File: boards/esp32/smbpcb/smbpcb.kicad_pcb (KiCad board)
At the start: 2 copper layers, 72.1 x 53.3 mm, 54 parts, among them IC1 MiCS-6814, J1 USB_B_Micro, Q1 SUD08P06-155L, Q2 SS8050_NPN, Q3 SS8050_NPN, U1 MCP73831-2-OT, U2 TPS61200DRC, U3 ESP32-WROOM-32, U4 SSD1306, U5 BME680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

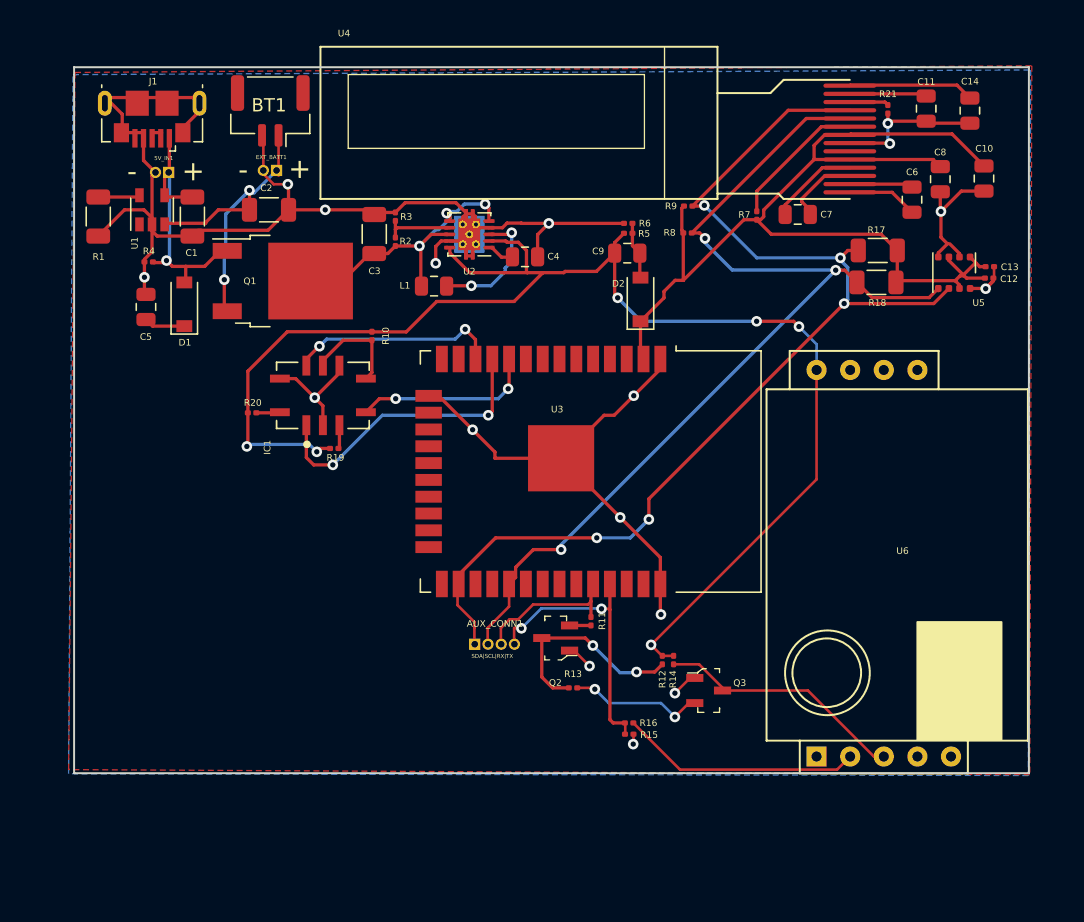
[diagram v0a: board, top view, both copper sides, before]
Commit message: pms7003 time
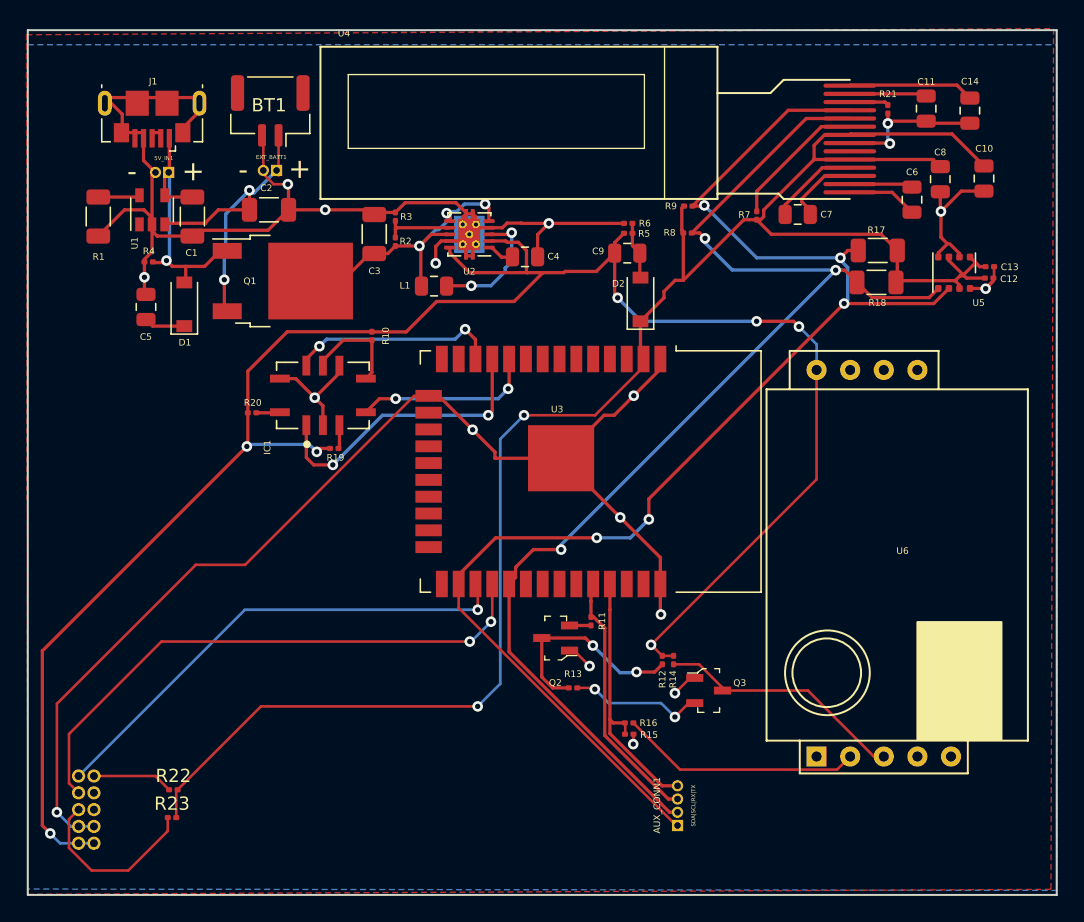
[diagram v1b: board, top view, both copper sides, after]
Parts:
- added J2: PMS7003, mics:PMS7003, F.Cu at (96.3, 63.3)
- added R22: 10k, Capacitor_SMD:C_0201_0603Metric, F.Cu at (85.2, 72.3)
- added R23: 10k, Capacitor_SMD:C_0201_0603Metric, F.Cu at (85.1, 74.4)
- moved AUX_CONN1 20.6 mm to (123.3, 75.0), turned to 180 degrees
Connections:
- net ESP_RX renamed ESP_RX0
- net ESP_TX renamed ESP_TX0
- U3 pad 27: unconnected-(U3-Pad27) -> ESP_TX1
- U3 pad 28: unconnected-(U3-Pad28) -> ESP_RX1
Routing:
- net +3V3: track 78.5 -> 140.5 mm, vias 0 -> 2
- net GND: track 160.2 -> 209.3 mm, vias 17 -> 18
- net ESP_RX1: track 0.00 -> 43.0 mm, vias 0 -> 2
- net +5V: track 108.2 -> 147.8 mm, vias 6 -> 7
- net ESP_TX1: track 0.00 -> 37.4 mm, vias 0 -> 1
- net SDA: track 86.1 -> 106.1 mm
- net SCL: track 77.7 -> 95.4 mm
- net Net-(J2-Pad5): track 0.00 -> 13.6 mm
- net ESP_RX0: track 11.2 -> 19.3 mm
- net Net-(J2-Pad10): track 0.00 -> 6.11 mm
- net ESP_TX0: track 21.5 -> 20.2 mm, vias 2 -> 0
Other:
- board size 72.1 x 53.3 mm -> 77.7 x 65.3 mm

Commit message: more work'
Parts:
- added ?: , , F.Cu at (74.1, 78.1)
- added AUX_CONN2: Conn_01x04_Female, Connector_PinHeader_1.00mm:PinHeader_1x04_P1.00mm_Vertical, F.Cu at (127.0, 75.0)
- added AUX_CONN3: Conn_01x04_Female, Connector_PinHeader_1.00mm:PinHeader_1x04_P1.00mm_Vertical, F.Cu at (130.6, 75.0)
- added AUX_CONN4: Conn_01x04_Female, Connector_PinHeader_1.00mm:PinHeader_1x04_P1.00mm_Vertical, F.Cu at (133.9, 75.0)
- added C15: 1nF, Capacitor_SMD:C_0201_0603Metric, F.Cu at (101.9, 52.9)
- added C16: 1nF, Capacitor_SMD:C_0201_0603Metric, F.Cu at (84.5, 50.6)
- added D3: PWR_LED, LED_SMD:LED_0805_2012Metric, F.Cu at (88.2, 39.8)
- added D4: PWR_LED, LED_SMD:LED_0805_2012Metric, F.Cu at (80.2, 39.8)
- added D5: D_Schottky, Diode_SMD:D_SOD-123, F.Cu at (80.2, 23.9)
- added R24: 470, Capacitor_SMD:C_0201_0603Metric, F.Cu at (101.8, 55.4)
- added R25: 2k, Capacitor_SMD:C_0201_0603Metric, F.Cu at (91.0, 39.2)
- added R26: 470, Capacitor_SMD:C_0201_0603Metric, F.Cu at (85.4, 48.5)
- added R27: 5.1k, Capacitor_SMD:C_0201_0603Metric, F.Cu at (101.8, 57.7)
- added R28: 470, Capacitor_SMD:C_0201_0603Metric, F.Cu at (83.3, 39.9)
- added REF**: MountingHole_3.2mm_M3_ISO7380_Pad, mountingholes:MountingHole_3.2mm_M3_ISO7380_Pad, F.Cu at (148.5, 16.5)
- added REF**: MountingHole_3.2mm_M3_ISO7380_Pad, mountingholes:MountingHole_3.2mm_M3_ISO7380_Pad, F.Cu at (147.7, 77.9)
- added REF**: MountingHole_3.2mm_M3_ISO7380_Pad, mountingholes:MountingHole_3.2mm_M3_ISO7380_Pad, F.Cu at (73.6, 16.6)
- added SW1: RESET, Button_Switch_SMD:SW_SPST_Omron_B3FS-101xP, F.Cu at (95.2, 54.8)
- added SW2: RESET, Button_Switch_SMD:SW_SPST_Omron_B3FS-101xP, F.Cu at (84.3, 54.9)
- BT1: footprint Connector_JST:JST_GH_SM02B-GHS-TB_1x02-1MP_P1.25mm_Horizontal -> Connector_JST:JST_EH_S2B-EH_1x02_P2.50mm_Horizontal
- R1: value 10k -> 2k
- moved J1 11.0 mm to (73.2, 25.1), turned to -90 degrees
- moved 5V_IN1 8.02 mm to (77.0, 24.2), turned to 0 degrees
- moved EXT_BATT1 4.12 mm to (91.3, 21.8), turned to 90 degrees
- moved R1 3.62 mm to (79.5, 32.6), turned to 0 degrees
- moved BT1 2.72 mm to (90.5, 19.1), turned to 0 degrees
- moved C2 0.22 mm to (92.5, 28.7)
- moved U1 0.15 mm to (83.5, 28.4)
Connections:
- AUX_CONN1 pad 3: ESP_RX0 -> ESP_TX0
- AUX_CONN1 pad 4: ESP_TX0 -> ESP_RX0
- C1 pad 1: Net-(5V_IN1-Pad1) -> Net-(C1-Pad1)
- D1 pad 2: Net-(5V_IN1-Pad1) -> Net-(C1-Pad1)
- J2 pad 7: ESP_RX1 -> ESP_RX2
- J2 pad 9: ESP_TX1 -> ESP_TX2
- Q1 pad 1: Net-(5V_IN1-Pad1) -> Net-(C1-Pad1)
- R11 pad 1: ESP_RX0 -> ESP_RX1
- R15 pad 2: ESP_TX0 -> ESP_TX1
- R16 pad 1: ESP_TX0 -> ESP_TX1
- R4 pad 1: Net-(5V_IN1-Pad1) -> Net-(C1-Pad1)
- U1 pad 1: unconnected-(U1-Pad1) -> Net-(D4-Pad1)
- U1 pad 4: Net-(5V_IN1-Pad1) -> Net-(C1-Pad1)
- U3 pad 10: NH3 -> unconnected-(U3-Pad10)
- U3 pad 11: NO2 -> unconnected-(U3-Pad11)
- U3 pad 12: CO -> unconnected-(U3-Pad12)
- U3 pad 25: unconnected-(U3-Pad25) -> IO0
- U3 pad 27: ESP_TX1 -> ESP_TX2
- U3 pad 28: ESP_RX1 -> ESP_RX2
- U3 pad 3: unconnected-(U3-Pad3) -> EN
- U3 pad 36: unconnected-(U3-Pad36) -> ESP_TX1
- U3 pad 37: unconnected-(U3-Pad37) -> ESP_RX1
- U3 pad 6: unconnected-(U3-Pad6) -> CO
- U3 pad 8: unconnected-(U3-Pad8) -> NH3
- U3 pad 9: unconnected-(U3-Pad9) -> NO2
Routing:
- net +3V3: track 140.5 -> 186.7 mm, vias 2 -> 3
- net ESP_RX2: track 0.00 -> 43.0 mm, vias 0 -> 2
- net EN: track 0.00 -> 38.1 mm, vias 0 -> 2
- net ESP_TX2: track 0.00 -> 37.4 mm, vias 0 -> 1
- net ESP_RX1: track 43.0 -> 5.72 mm, vias 2 -> 0
- net Net-(C1-Pad1): track 0.00 -> 29.1 mm, vias 0 -> 4
- net GND: track 209.3 -> 237.9 mm, vias 18 -> 19
- net ESP_TX1: track 37.4 -> 11.9 mm, vias 1 -> 2
- net Net-(5V_IN1-Pad1): track 20.6 -> 4.37 mm, vias 1 -> 0
- net Net-(D4-Pad1): track 0.00 -> 12.2 mm, vias 0 -> 2
- net SCL: track 95.4 -> 107.0 mm
- net SDA: track 106.1 -> 117.7 mm
- net +5V: track 147.8 -> 137.8 mm, vias 7 -> 5
- net CO: track 15.5 -> 23.1 mm
- net Net-(C16-Pad2): track 0.00 -> 7.12 mm
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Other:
- board size 77.7 x 65.3 mm -> 81.9 x 69.8 mm
- board text added: "CHG_LED"
- board text added: "IO0"
- board text added: "PWR_LED"
- board text added: "SDA|SCL|3V3|GND"
- board text added: "SDA|SCL|5V|GND"
- board text added: "SDA|SCL|TX|RX"
- board text removed: "SDA|SCL|RX|TX"

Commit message: ordering dis
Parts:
- R17, R18: footprint Capacitor_SMD:C_1206_3216Metric -> Capacitor_SMD:C_0805_2012Metric
- R22, R23, R27, R4, R7, R8, R9: footprint Capacitor_SMD:C_0201_0603Metric -> Capacitor_SMD:C_0805_2012Metric
- moved R27 1.65 mm to (101.8, 59.4)
- moved R8 0.91 mm to (123.7, 31.1)
- moved R9 0.79 mm to (123.8, 28.9)
- moved R4 0.55 mm to (83.7, 32.0)
- moved D3 0.31 mm to (88.3, 40.0)
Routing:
- net GND: track 237.9 -> 252.2 mm
- net +5V: track 137.8 -> 130.9 mm, vias 5 -> 11
- net +3V3: track 186.7 -> 188.7 mm
- net IO0: track 5.74 -> 7.03 mm
- net SCL: track 107.0 -> 105.8 mm

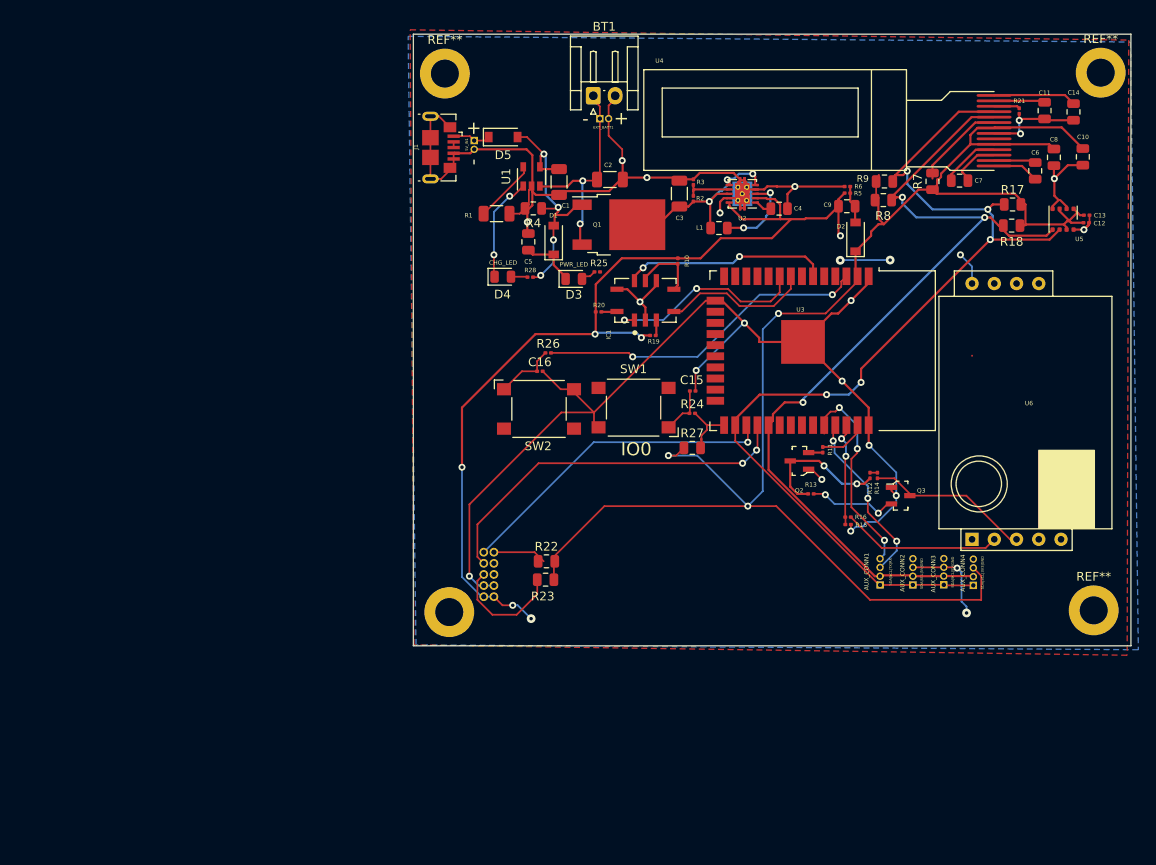
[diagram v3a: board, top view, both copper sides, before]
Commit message: added decoupling cap to 3v3 off of esp32 board
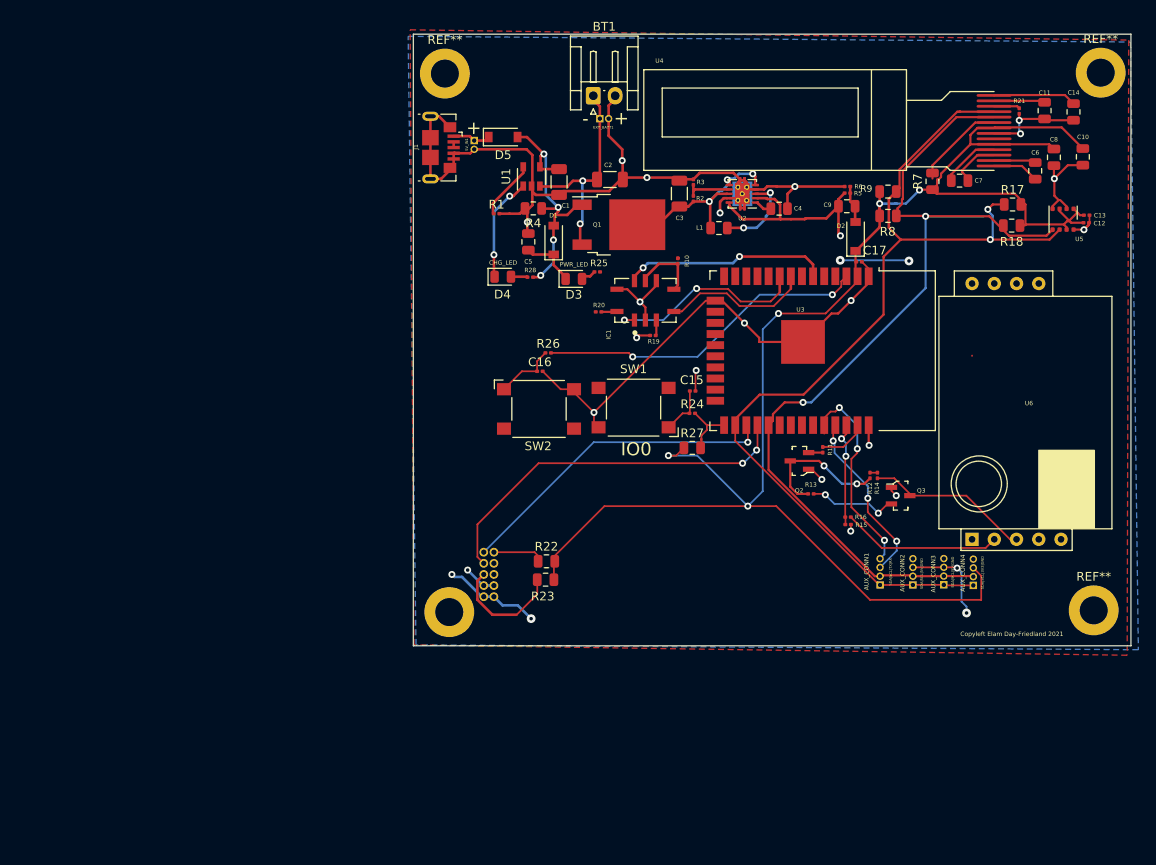
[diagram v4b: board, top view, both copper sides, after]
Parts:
- added C17: 10uF, Capacitor_SMD:C_0201_0603Metric, F.Cu at (120.9, 38.1)
- R1: footprint Capacitor_SMD:C_1206_3216Metric -> Capacitor_SMD:C_0201_0603Metric
- moved R8 1.88 mm to (124.2, 32.9)
- moved R9 1.22 mm to (124.2, 30.1)
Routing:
- net +5V: track 130.9 -> 56.4 mm, vias 11 -> 8
- net GND: track 252.2 -> 191.9 mm
- net SCL: track 105.8 -> 111.1 mm, vias 3 -> 2
- net SDA: track 117.7 -> 114.8 mm, vias 5 -> 2
- net +3V3: track 188.7 -> 187.4 mm, vias 3 -> 5
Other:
- board text added: "Copyleft Elam Day-Friedland 2021"

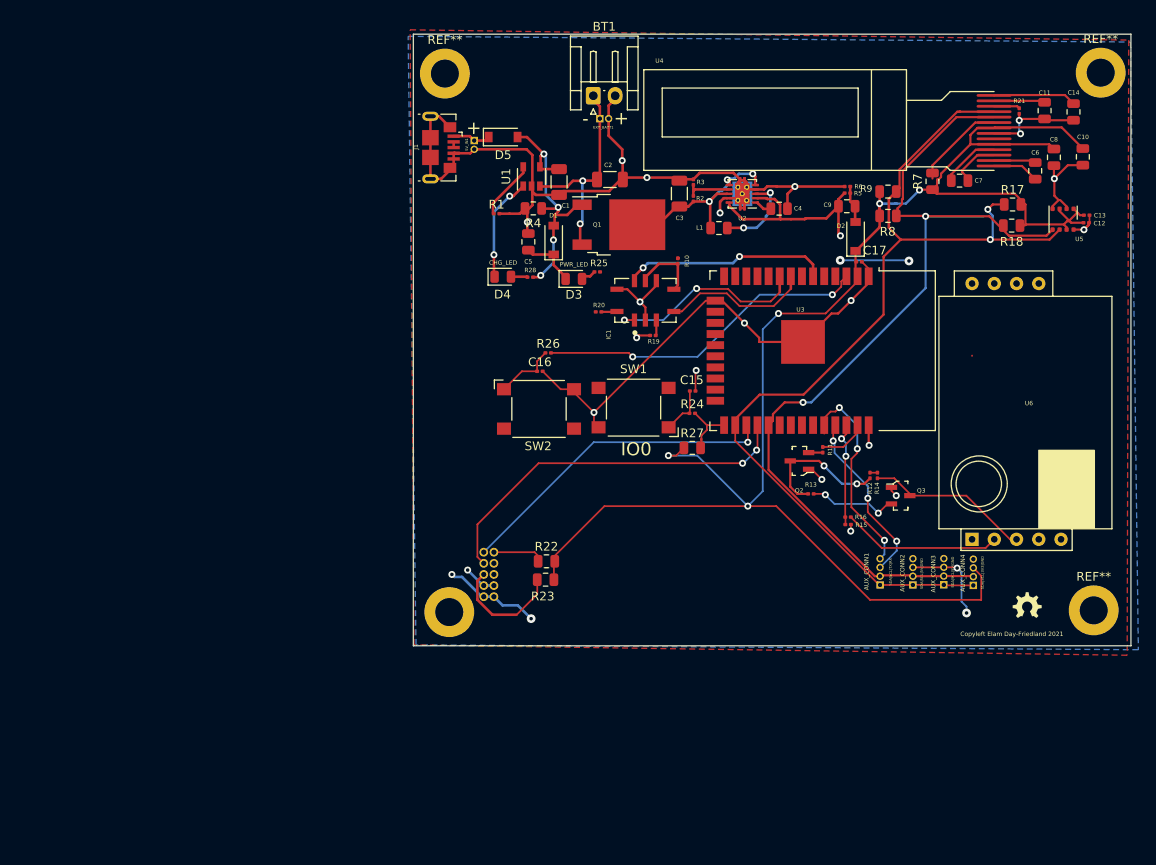
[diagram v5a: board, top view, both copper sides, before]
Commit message: made everything 0805 or bigger except that nagging BGA Linear regulator and the bme680
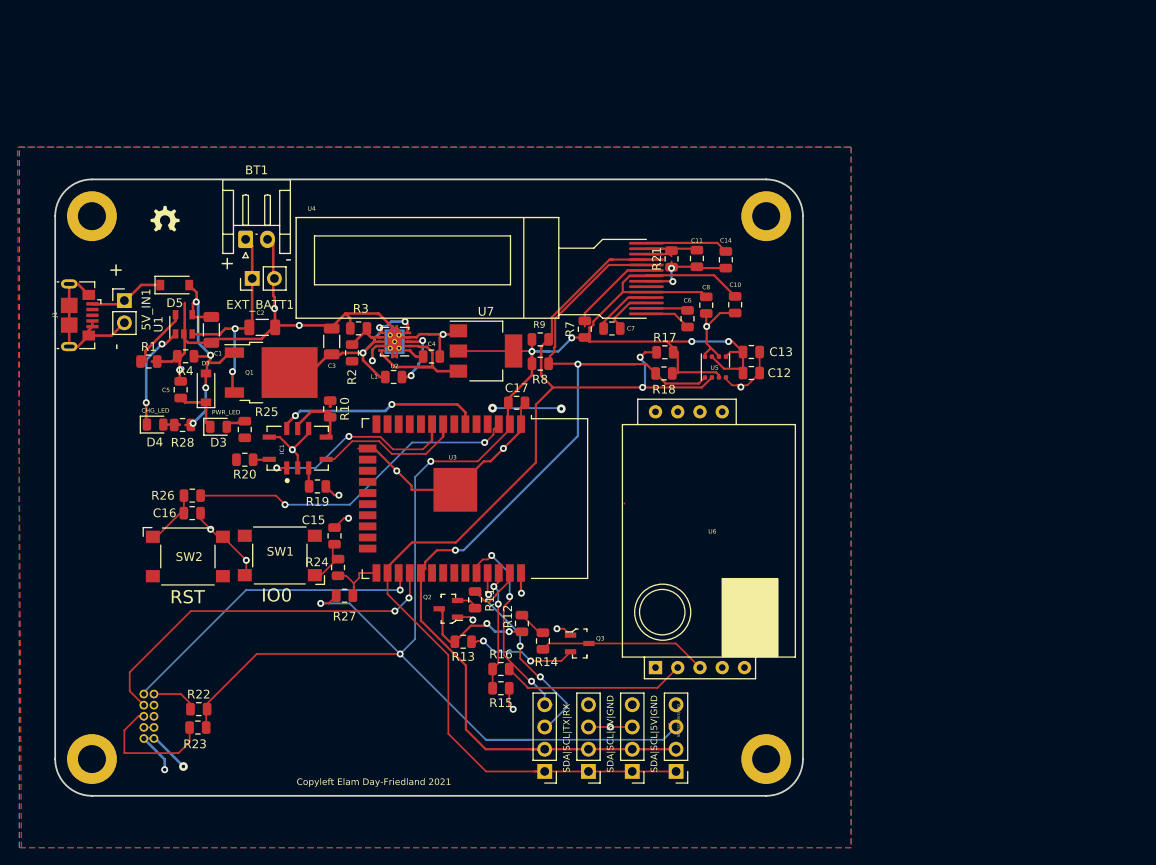
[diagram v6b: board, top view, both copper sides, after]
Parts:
- removed C9: 22pF, Capacitor_SMD:C_0805_2012Metric
- removed D2: D, Diode_SMD:D_SOD-123
- removed R5: 1k, Capacitor_SMD:C_0201_0603Metric
- removed R6: 2k, Capacitor_SMD:C_0201_0603Metric
- removed the REF** at (148.5, 16.5)
- removed the REF** at (147.7, 77.9)
- removed the REF** at (73.6, 16.6)
- added MOUNT4: MountingHole_3.2mm_M3_ISO7380_Pad, MountingHole:MountingHole_3.2mm_M3_ISO7380_Pad, F.Cu at (110.3, 94.9)
- added REF**: MountingHole_3.2mm_M3_ISO7380_Pad, MountingHole:MountingHole_3.2mm_M3_ISO7380_Pad, F.Cu at (110.3, 32.9)
- added REF**: MountingHole_3.2mm_M3_ISO7380_Pad, MountingHole:MountingHole_3.2mm_M3_ISO7380_Pad, F.Cu at (33.3, 32.9)
- added U7: AMS1117-3.3, Package_TO_SOT_SMD:SOT-223-3_TabPin2, F.Cu at (78.3, 48.3)
- 5V_IN1, EXT_BATT1: footprint Connector_PinHeader_1.00mm:PinHeader_1x02_P1.00mm_Vertical -> Connector_PinHeader_2.54mm:PinHeader_1x02_P2.54mm_Vertical
- AUX_CONN1, AUX_CONN2, AUX_CONN3, AUX_CONN4: footprint Connector_PinHeader_1.00mm:PinHeader_1x04_P1.00mm_Vertical -> Connector_PinHeader_2.54mm:PinHeader_1x04_P2.54mm_Vertical
- C12, C13: value .1uF -> 100nF; footprint Capacitor_SMD:C_0201_0603Metric -> Capacitor_SMD:C_0805_2012Metric
- C15, C16, C17, R1, R10, R11, R12, R13, R14, R15, R16, R19, R2, R20, R21, R24, R25, R26, R28, R3: footprint Capacitor_SMD:C_0201_0603Metric -> Capacitor_SMD:C_0805_2012Metric
- moved J1 45.5 mm to (31.9, 44.2)
- moved C15 44.1 mm to (61.0, 69.4), turned to -90 degrees
- moved R24 44.1 mm to (61.4, 73.0), turned to -90 degrees
- moved R25 44.1 mm to (50.8, 57.2), turned to -90 degrees
- moved D3 43.9 mm to (47.8, 56.9)
- moved 5V_IN1 43.9 mm to (37.0, 42.5)
- moved R15 43.8 mm to (80.0, 86.8)
- moved AUX_CONN1 43.8 mm to (85.0, 96.3)
- moved R26 43.8 mm to (44.8, 64.8)
- moved R20 43.8 mm to (50.8, 60.7)
- moved SW1 43.8 mm to (54.8, 71.6)
- moved EXT_BATT1 43.7 mm to (51.6, 40.0)
- moved Q2 43.5 mm to (74.0, 77.7)
- moved SW2 43.5 mm to (44.2, 71.8)
- moved R16 43.3 mm to (80.0, 84.6)
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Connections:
- ? pad 1: (no net) -> GND
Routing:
- net +3V3: track 187.4 -> 213.6 mm, vias 5 -> 7
- net GND: track 191.9 -> 171.1 mm
- net SDA: track 114.8 -> 129.1 mm
- net SCL: track 111.1 -> 124.0 mm
- net +5V: track 56.4 -> 45.0 mm, vias 8 -> 6
- net Net-(C9-Pad2): track 4.28 -> 0.00 mm
- net Net-(5V_IN1-Pad1): track 4.37 -> 8.59 mm
- net Net-(R16-Pad2): track 18.3 -> 21.2 mm
- net ESP_TX0: track 20.4 -> 23.3 mm
- net Net-(Q3-Pad2): track 10.2 -> 12.7 mm
- net Net-(L1-Pad2): track 10.1 -> 7.72 mm
- net ESP_RX1: track 5.72 -> 8.05 mm
- net Net-(Q2-Pad3): track 15.8 -> 13.5 mm
- net ESP_TX1: track 11.9 -> 14.0 mm
- net Net-(C3-Pad1): track 20.0 -> 22.0 mm
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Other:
- board size 81.9 x 69.8 mm -> 85.4 x 70.4 mm
- board text added: "RST"
